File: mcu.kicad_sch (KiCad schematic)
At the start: 26 parts, among them J1 Conn_ARM_JTAG_SWD_20, J3 Conn_01x09_Socket, SW1 SW_SPST, U10 WE-TVS-824015043, U6 STM32F469VETx

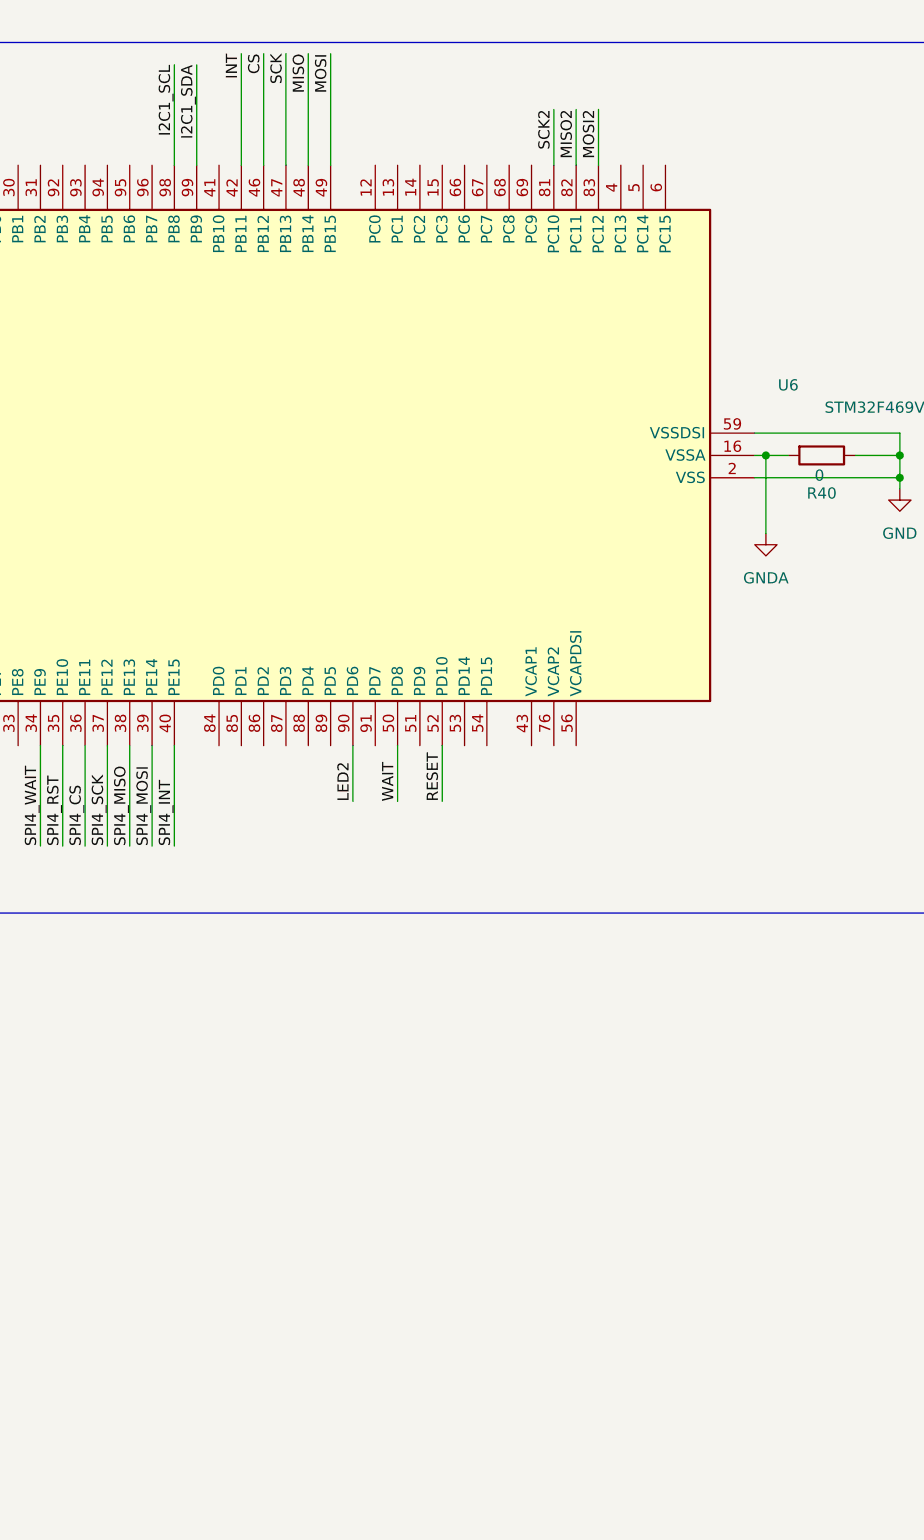
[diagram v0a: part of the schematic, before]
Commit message: added HSE
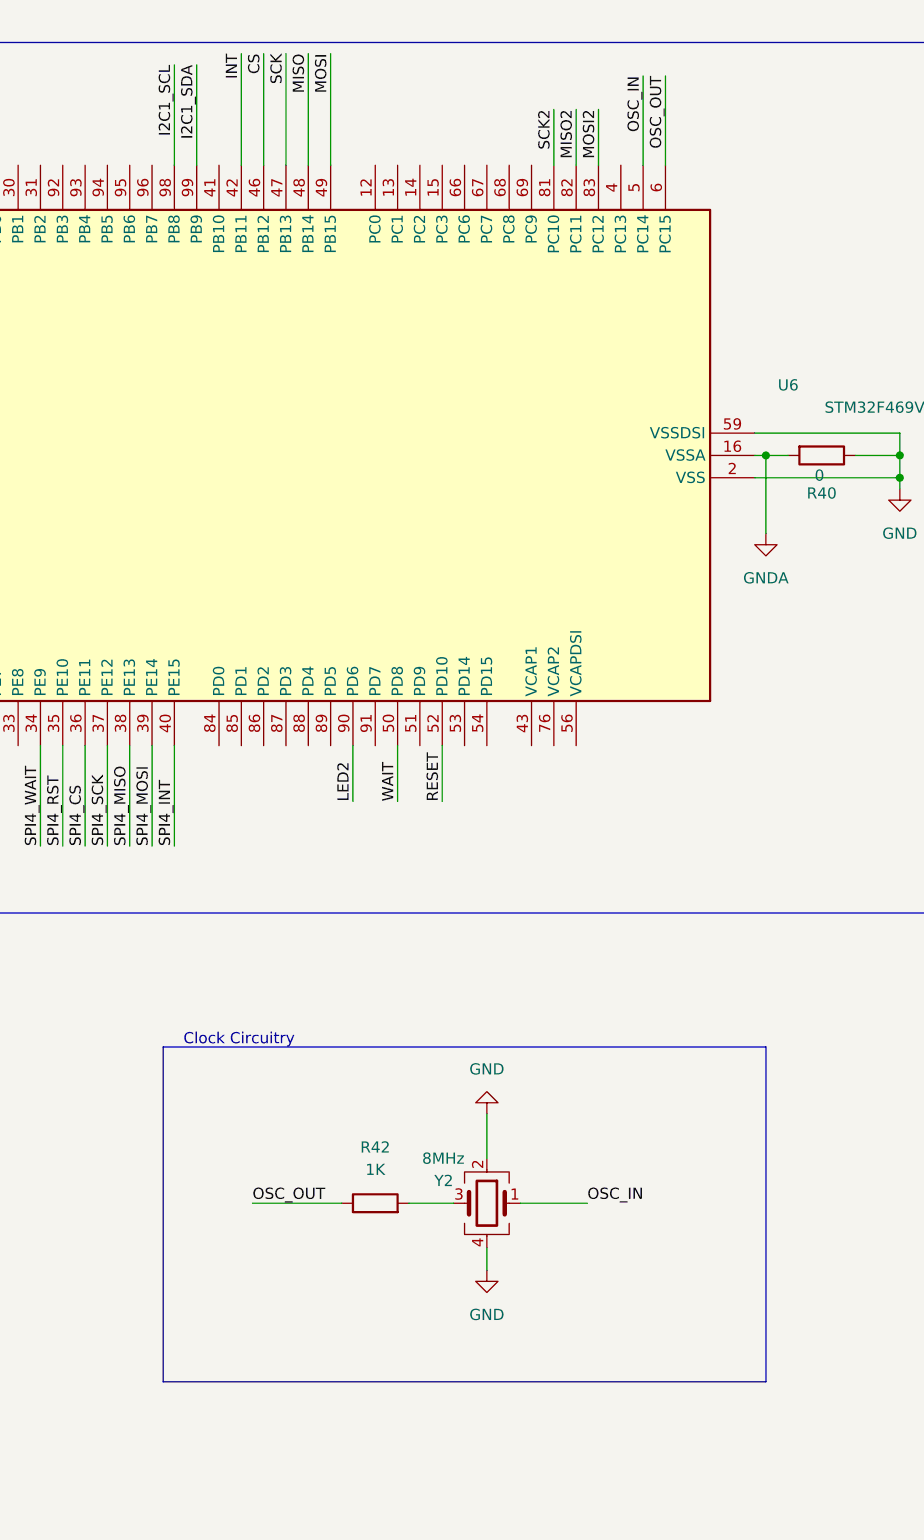
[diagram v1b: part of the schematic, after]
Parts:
- added R42: 1K, Resistor_SMD:R_0805_2012Metric, symbol Device:R
- added Y2: 8MHz, Crystal:Crystal_SMD_SeikoEpson_FA238-4Pin_3.2x2.5mm, symbol Device:Crystal_GND24
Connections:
- net GND: now also Y2.2, Y2.4
- net OSC_IN: now reaches U6.5 (PC14)
- net OSC_IN: now also Y2.1
- net OSC_OUT: now reaches U6.6 (PC15)
- net OSC_OUT: now also R42.1
- new net: R42.2, Y2.3
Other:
- note added: "Clock Circuitry"

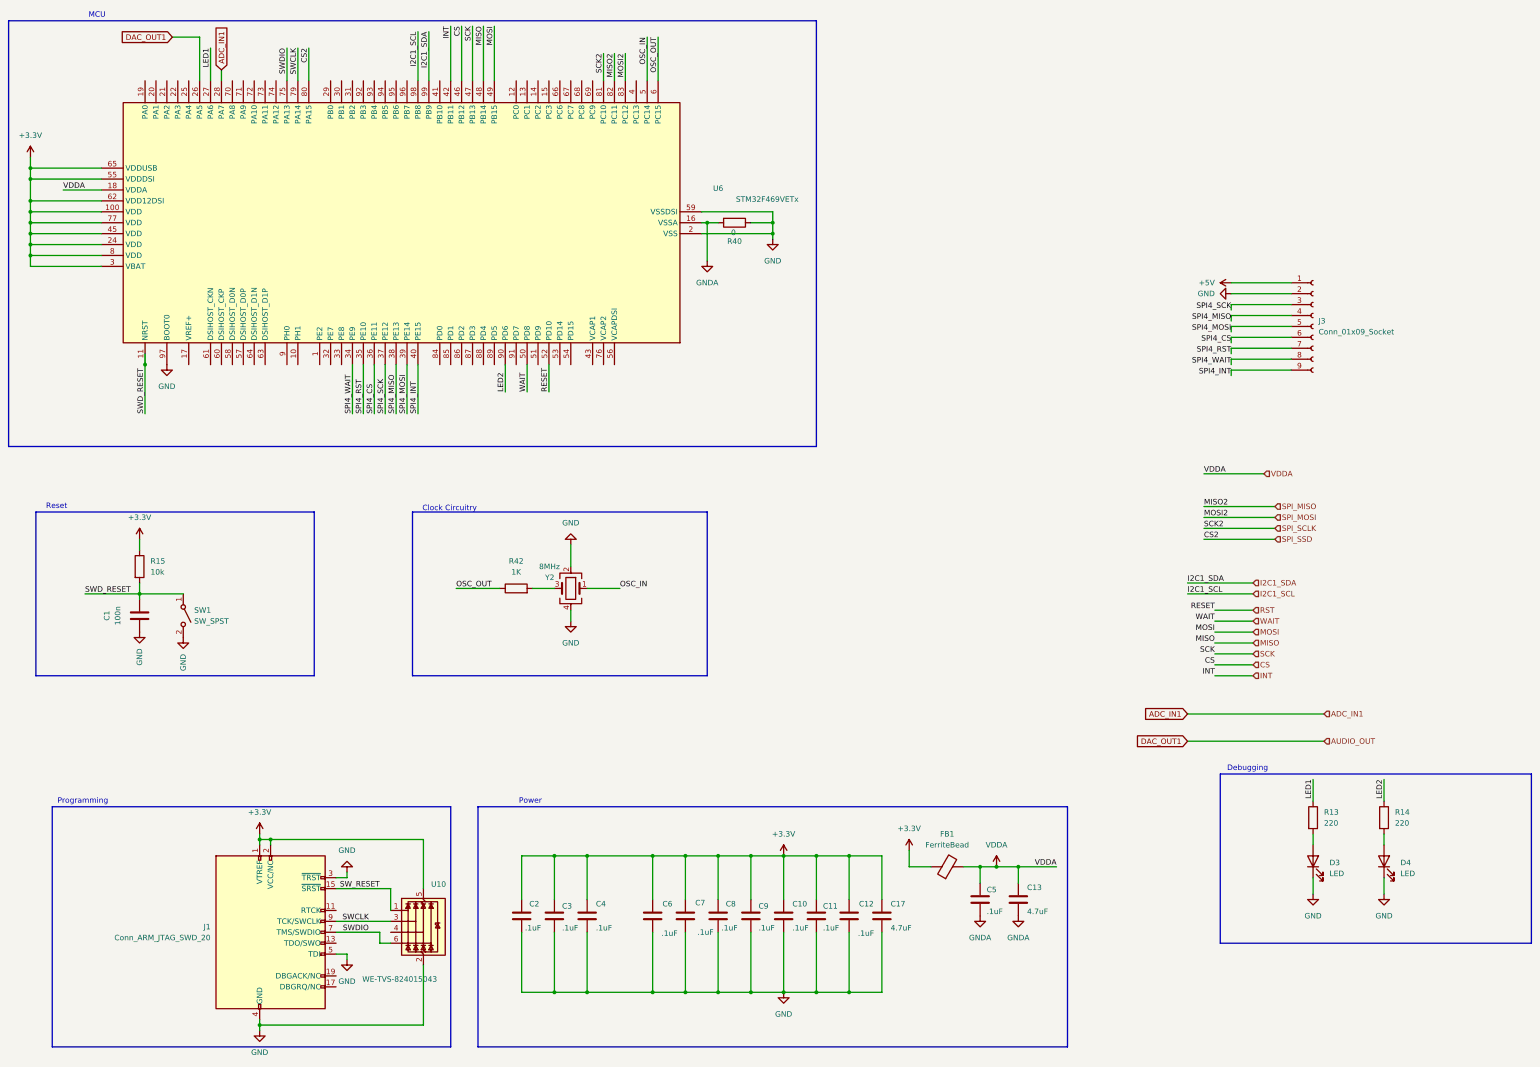
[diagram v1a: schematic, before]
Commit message: added HE2 and expanded VDDA plane
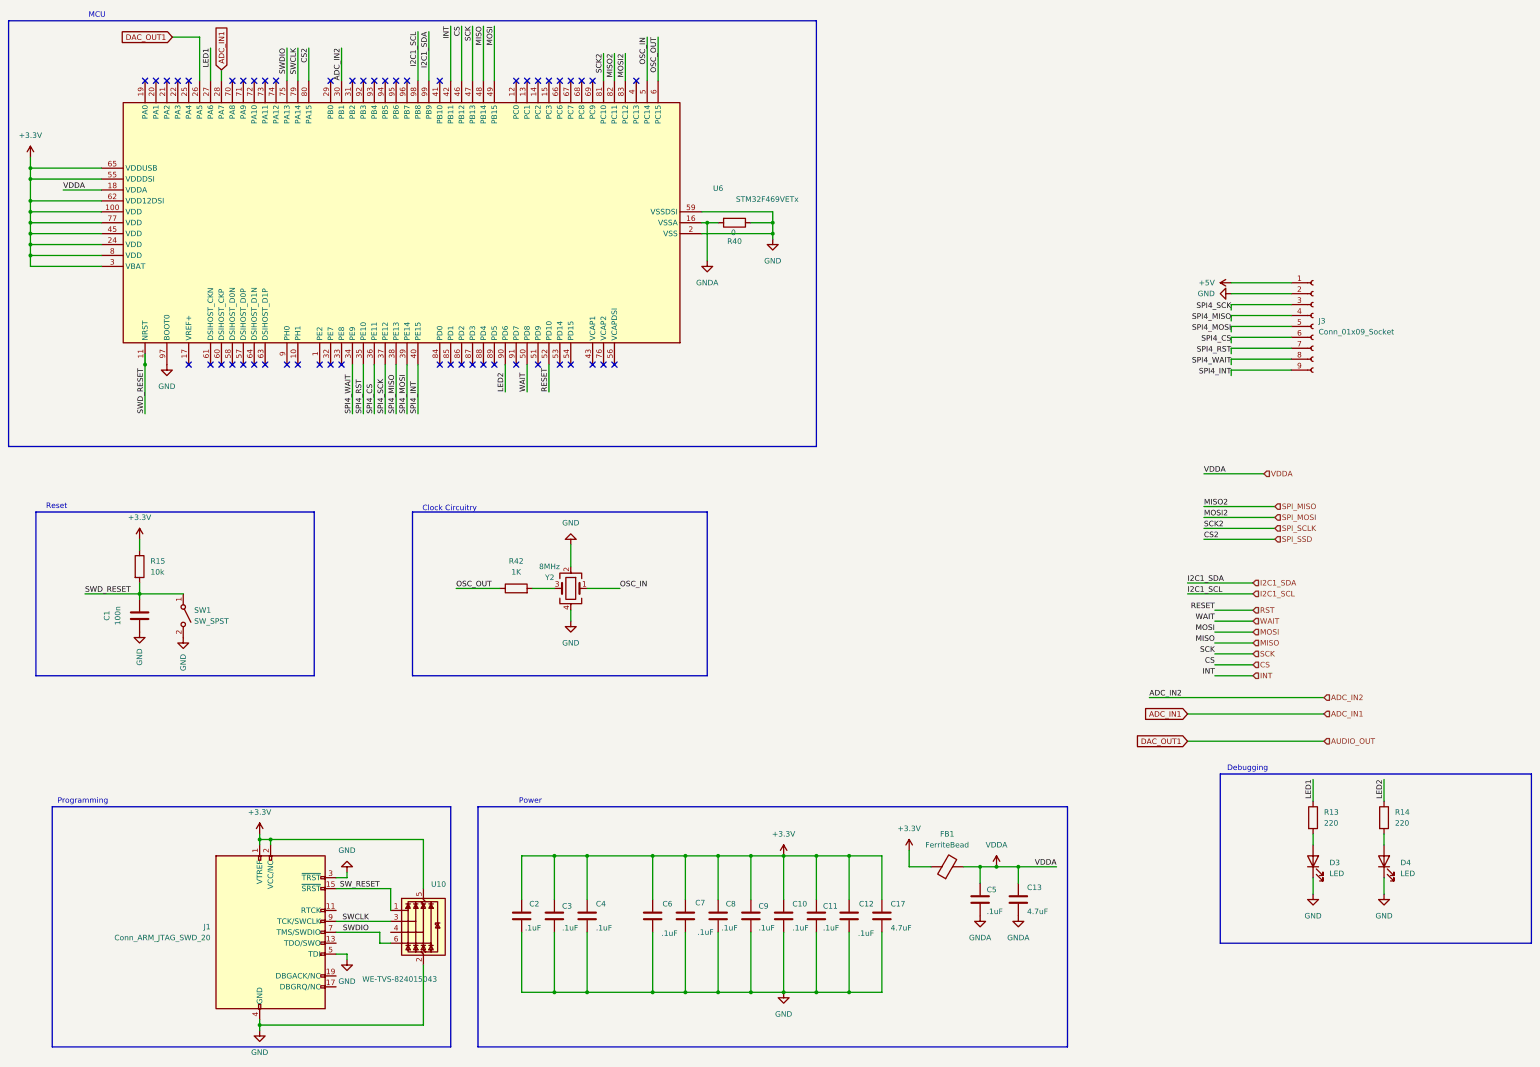
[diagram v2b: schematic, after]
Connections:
- net ADC_IN2: now reaches U6.30 (PB1)
- no-connect marks 0 -> 52
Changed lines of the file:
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@@
 		(color 0 0 0 0)
 	)
+	(no_connect
+		(at 143.51 44.45)
+	)
+	(no_connect
+		(at 128.27 110.49)
+	)
+	(no_connect
+		(at 123.19 110.49)
+	)
+	(no_connect
+		(at 87.63 110.49)
+	)
+	(no_connect
+		(at 74.93 110.49)
+	)
+	(no_connect
+		(at 146.05 44.45)
+	)
+	(no_connect
+		(at 125.73 110.49)
+	)
+	(no_connect
+		(at 92.71 110.49)
+	)
+	(no_connect
+		(at 113.03 44.45)
+	)
+	(no_connect
+		(at 80.01 110.49)
+	)
+	(no_connect
+		(at 120.65 110.49)
+	)
+	(no_connect
+		(at 151.13 110.49)
+	)
+	(no_connect
+		(at 158.75 110.49)
+	)
+	(no_connect
+		(at 52.07 44.45)
+	)
+	(no_connect
+		(at 82.55 44.45)
+	)
+	(no_connect
+		(at 166.37 44.45)
+	)
+	(no_connect
+		(at 140.97 44.45)
+	)
+	(no_connect
+		(at 151.13 44.45)
+	)
+	(no_connect
+		(at 138.43 110.49)
+	)
+	(no_connect
+		(at 107.95 44.45)
+	)
+	(no_connect
+		(at 100.33 44.45)
+	)
+	(no_connect
+		(at 130.81 110.49)
+	)
+	(no_connect
+		(at 57.15 44.45)
+	)
+	(no_connect
+		(at 133.35 110.49)
+	)
+	(no_connect
+		(at 102.87 44.45)
+	)
+	(no_connect
+		(at 69.85 110.49)
+	)
+	(no_connect
+		(at 54.61 44.45)
+	)
+	(no_connect
+		(at 62.23 44.45)
+	)
+	(no_connect
+		(at 148.59 44.45)
+	)
+	(no_connect
+		(at 67.31 110.49)
+	)
+	(no_connect
+		(at 74.93 44.45)
+	)
+	(no_connect
+		(at 156.21 110.49)
+	)
+	(no_connect
+		(at 97.79 110.49)
+	)
+	(no_connect
+		(at 95.25 110.49)
+	)
+	(no_connect
+		(at 138.43 44.45)
+	)
+	(no_connect
+		(at 72.39 44.45)
+	)
+	(no_connect
+		(at 77.47 44.45)
+	)
+	(no_connect
+		(at 85.09 110.49)
+	)
+	(no_connect
+		(at 148.59 110.49)
+	)
+	(no_connect
+		(at 161.29 110.49)
+	)
+	(no_connect
+		(at 62.23 110.49)
+	)
+	(no_connect
+		(at 59.69 44.45)
+	)
+	(no_connect
+		(at 143.51 110.49)
+	)
+	(no_connect
+		(at 156.21 44.45)
+	)
+	(no_connect
+		(at 153.67 44.45)
+	)
+	(no_connect
+		(at 80.01 44.45)
+	)
+	(no_connect
+		(at 72.39 110.49)
+	)
+	(no_connect
+		(at 95.25 44.45)
+	)
+	(no_connect
+		(at 105.41 44.45)
+	)
+	(no_connect
+		(at 110.49 44.45)
+	)
+	(no_connect
+		(at 120.65 44.45)
+	)
+	(no_connect
+		(at 77.47 110.49)
+	)
 	(wire
 		(pts
@@
 	(wire
 		(pts
+			(xy 97.79 36.83) (xy 97.79 44.45)
+		)
+		(stroke
+			(width 0)
+			(type default)
+		)
+	)
+	(wire
+		(pts
 			(xy 200.66 224.79) (xy 200.66 234.95)
 		)
@@
 		(pts
 			(xy 300.99 175.26) (xy 309.88 175.26)
+		)
+		(stroke
+			(width 0)
+			(type default)
+		)
+	)
+	(wire
+		(pts
+			(xy 326.39 187.96) (xy 285.75 187.96)
 		)
 		(stroke
@@
 		)
 	)
+	(label "ADC_IN2"
+		(at 285.75 187.96 0)
+		(effects
+			(font
+				(size 1.27 1.27)
+			)
+			(justify left bottom)
+		)
+	)
 	(label "CS"
 		(at 125.73 31.75 270)
@@
 			)
 			(justify left bottom)
+		)
+	)
+	(label "ADC_IN2"
+		(at 97.79 36.83 270)
+		(effects
+			(font
+				(size 1.27 1.27)
+			)
+			(justify right bottom)
 		)
 	)
@@
 		(effects
 			(font
+				(size 1.27 1.27)
+			)
+			(justify left)
+		)
+	)
+	(hierarchical_label "ADC_IN2"
+		(shape input)
+		(at 326.39 187.96 0)
+		(effects
+			(font

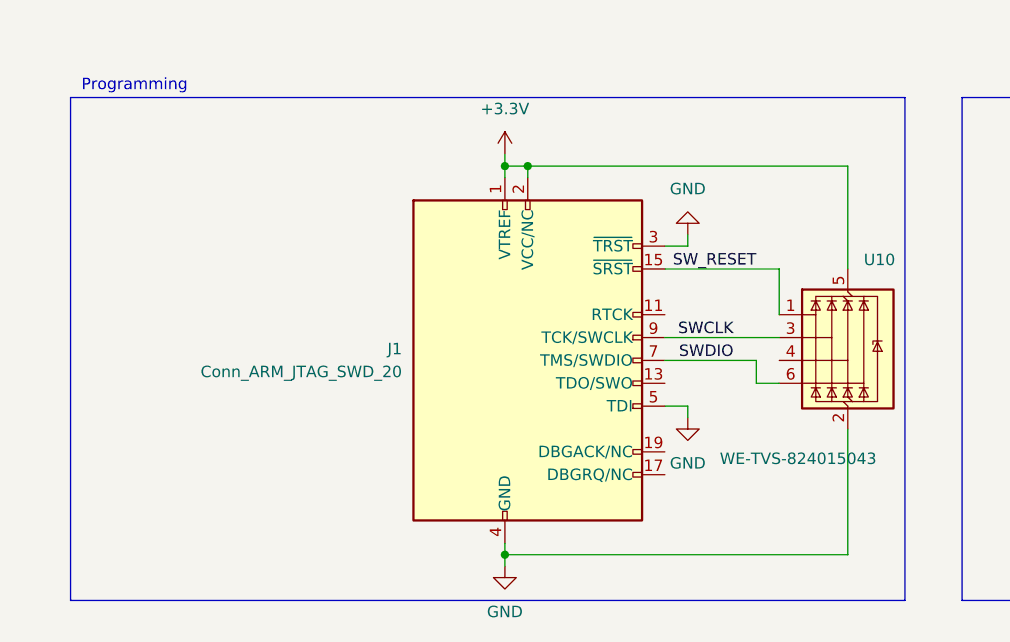
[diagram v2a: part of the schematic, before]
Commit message: added 10 pin stlink and fixed a bunch of errors and warnings
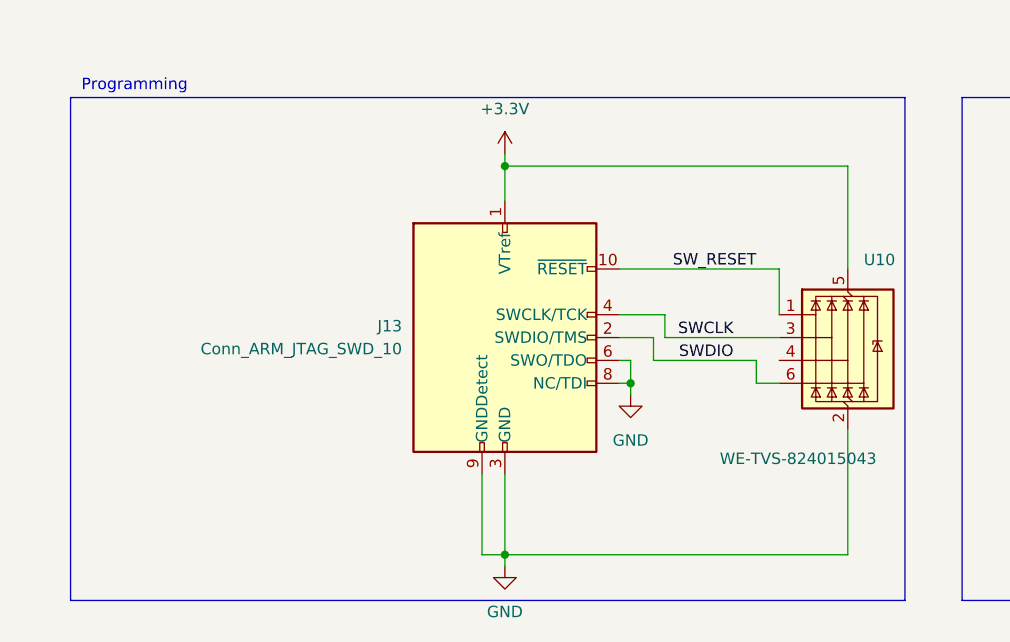
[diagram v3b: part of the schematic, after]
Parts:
- removed J1: Conn_ARM_JTAG_SWD_20, Connector_PinHeader_2.54mm:PinHeader_2x10_P2.54mm_Vertical, symbol Connector:Conn_ARM_JTAG_SWD_20
- added J13: Conn_ARM_JTAG_SWD_10, Connector_PinSocket_2.54mm:PinSocket_2x05_P2.54mm_Vertical, symbol Connector:Conn_ARM_JTAG_SWD_10
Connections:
- net +3.3V: now also J13.1 (VTref)
- net GND: now also J13.3 (GND), J13.5 (GND), J13.6 (SWO/TDO), J13.8 (NC/TDI), J13.9 (GNDDetect)
- net SWCLK: now also J13.4 (SWCLK/TCK)
- net SWDIO: now also J13.2 (SWDIO/TMS)
- net SW_RESET: now also J13.10 (~{RESET})
